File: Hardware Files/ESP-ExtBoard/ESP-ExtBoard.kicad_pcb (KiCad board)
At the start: 2 copper layers, 72.6 x 58.4 mm, 6 parts, among them J1 PIN_HEADER, J2 PIN_HEADER_1x4, U1 ESP32-DEVKIT-V1, U2 BME280, U3 MPU6050, U4 SSD1306

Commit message: [Hardware] V0.1 finished
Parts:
- moved U3 23.5 mm to (119.4, 84.0), turned to 90 degrees
- moved J2 2.04 mm to (127.0, 63.0)
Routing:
- net +3.3V: track 32.3 -> 126.0 mm
- net /UART2_RX: track 0.00 -> 79.4 mm
- net /VSPI_MOSI: track 0.00 -> 53.6 mm
- net /VSPI_CS: track 0.00 -> 43.4 mm
- net /VSPI_CLK: track 0.00 -> 43.4 mm
- net /VSPI_MISO: track 0.00 -> 43.4 mm
- net /I2C0_SDA: track 60.6 -> 49.6 mm
- net /I2C0_SCL: track 73.2 -> 75.1 mm
- net /UART2_TX: track 37.8 -> 36.6 mm
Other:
- board text added: "Zephyr ESP32 Breakout Board v 0.1 Design by Guilherme Freire"

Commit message: Signed-off-by: Freire <freireg1503@gmail.com>
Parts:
- added J3: PIN_HEADER, New_lib:PinHeader_1x06_P2.54mm_Vertical, F.Cu at (83.5, 100.8)
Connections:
- U1 pad 23: unconnected-(U1-D25-Pad23) -> /GPIO25
- U1 pad 24: unconnected-(U1-D26-Pad24) -> /GPIO26
- U1 pad 25: unconnected-(U1-D27-Pad25) -> /GPIO27
- U1 pad 26: unconnected-(U1-D14-Pad26) -> /GPIO14
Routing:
- net +3.3V: track 126.0 -> 162.2 mm
- net /GPIO26: track 0.00 -> 4.81 mm
- net /GPIO14: track 0.00 -> 4.81 mm
- net /GPIO27: track 0.00 -> 4.81 mm
- net /GPIO25: track 0.00 -> 4.81 mm
- net /UART2_RX: track 79.4 -> 77.0 mm
- net /I2C0_SDA: track 49.6 -> 50.9 mm
- net unconnected-(U1-VP-Pad17): track 1.08 -> 0.00 mm
- added copper zone on F.Cu, net Earth
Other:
- board text added: "D15 D26 D27 D14 GND VCC"
- board text added: "Zephyr ESP32 Breakout Board v 0.2 Design by Guilherme Freire"
- board text removed: "Zephyr ESP32 Breakout Board v 0.1 Design by Guilherme Freire"

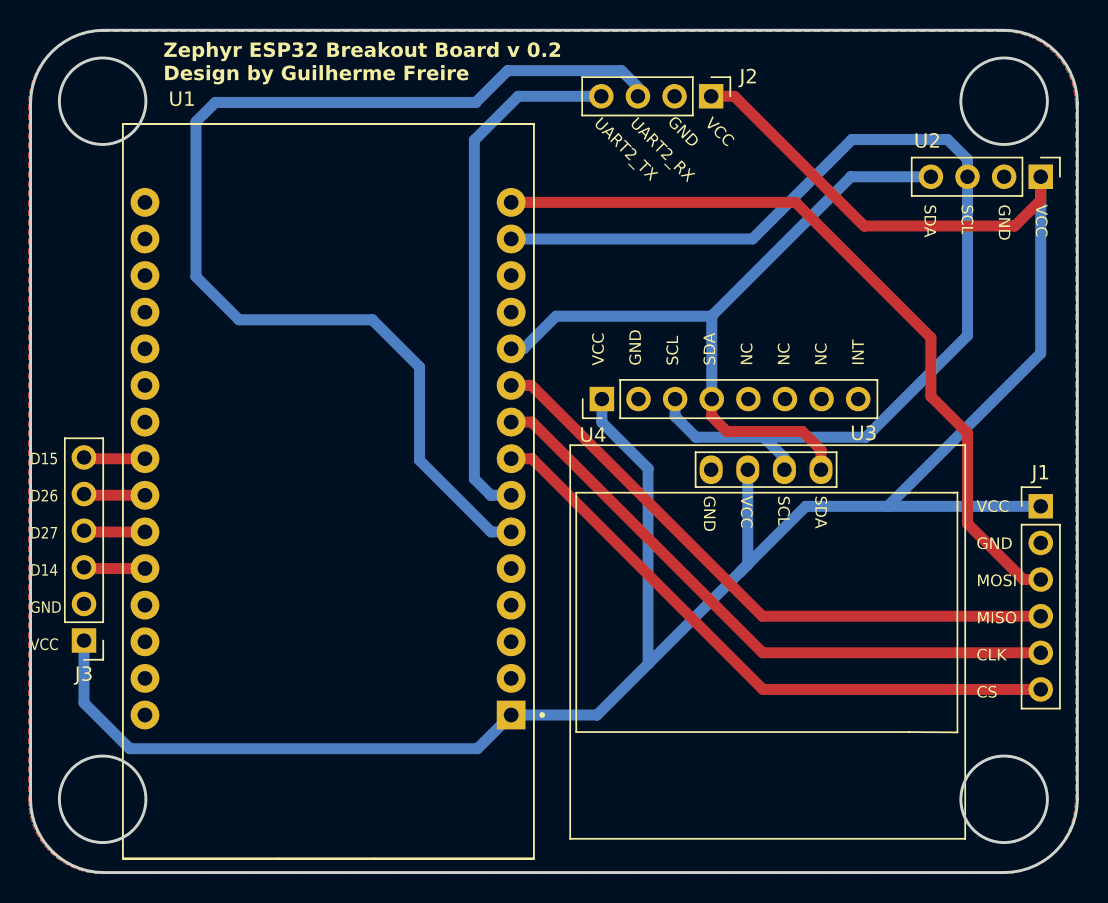
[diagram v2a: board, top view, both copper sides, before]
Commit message: [hardware] SD module pin update
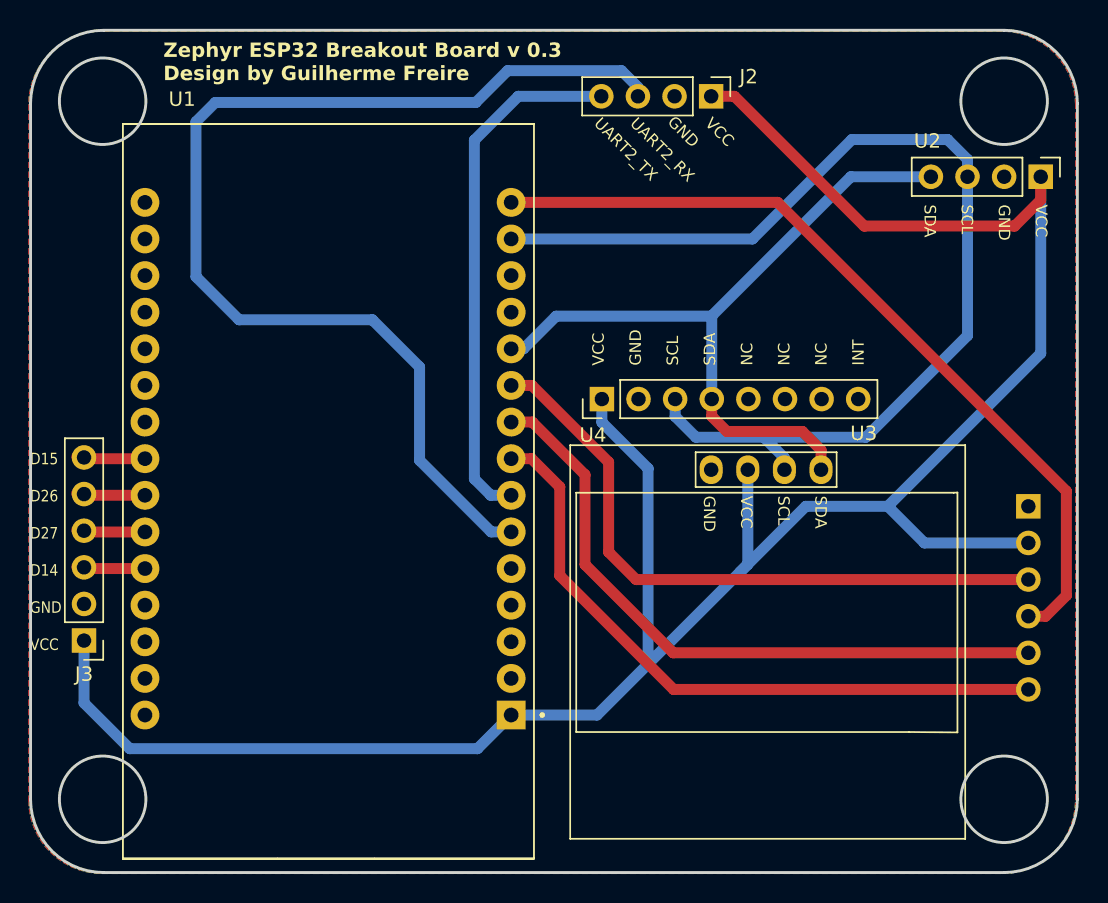
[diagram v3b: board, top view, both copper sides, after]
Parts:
- J1: footprint New_lib:PinHeader_1x06_P2.54mm_Vertical -> New_lib:PinHeader_1x06_P2.54mm_Vertical_1; moved to B.Cu
- moved J1 0.86 mm to (149.0, 91.4), turned to 180 degrees
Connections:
- J1 pad 1: +3.3V -> Earth
- J1 pad 2: Earth -> +3.3V
- J1 pad 3: /VSPI_MOSI -> /VSPI_MISO
- J1 pad 4: /VSPI_MISO -> /VSPI_MOSI
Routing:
- net /VSPI_MOSI: track 53.6 -> 57.3 mm
- net /VSPI_CLK: track 43.4 -> 46.2 mm
- net /VSPI_CS: track 43.4 -> 46.1 mm
- net /VSPI_MISO: track 43.4 -> 45.1 mm
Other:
- board text added: "GND VCC MISO MOSI CLK CS"
- board text added: "Zephyr ESP32 Breakout Board v 0.3 Design by Guilherme Freire"
- board text removed: "VCC GND MOSI MISO CLK CS"
- board text removed: "Zephyr ESP32 Breakout Board v 0.2 Design by Guilherme Freire"

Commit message: [hardware] minor updates
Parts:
- added J4: PIN_HEADER, New_lib:PinHeader_1x06_P2.54mm_Vertical, F.Cu at (83.5, 71.5)
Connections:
- U1 pad 19: unconnected-(U1-D34-Pad19) -> /GPIO34
- U1 pad 20: unconnected-(U1-D35-Pad20) -> /GPIO35
- U1 pad 21: unconnected-(U1-D32-Pad21) -> /GPIO32
- U1 pad 22: unconnected-(U1-D33-Pad22) -> /GPIO33
- U1 pad 30: unconnected-(U1-VIN-Pad30) -> +5V
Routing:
- net +5V: track 0.00 -> 49.0 mm
- net +3.3V: track 162.4 -> 173.9 mm
- net /GPIO35: track 0.00 -> 4.79 mm
- net /GPIO33: track 0.00 -> 4.79 mm
- net /GPIO32: track 0.00 -> 4.79 mm
- net /GPIO34: track 0.00 -> 4.79 mm
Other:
- board text added: "5V GND D34 D35 D32 D33"
- board text added: "Zephyr ESP32 Breakout Board v 0.5 Design by Guilherme Freire"
- board text removed: "Zephyr ESP32 Breakout Board v 0.3 Design by Guilherme Freire"

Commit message: [hardware] V1.0
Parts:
- moved J1 3.94 mm to (148.9, 87.5)
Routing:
- net +3.3V: track 173.9 -> 154.7 mm
- net /VSPI_MISO: track 45.1 -> 39.7 mm
- net /VSPI_CLK: track 46.2 -> 40.8 mm
- net /VSPI_CS: track 46.1 -> 40.8 mm
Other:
- outline, holes or cut-outs redrawn
- board text added: "BME280"
- board text added: "MPU6050"
- board text added: "OLED SSD1306"
- board text added: "SD CARD MODULE"
- board text added: "Zephyr ESP32 Breakout Board v 1.0 Design by Guilherme Freire"
- board text removed: "Zephyr ESP32 Breakout Board v 0.5 Design by Guilherme Freire"
